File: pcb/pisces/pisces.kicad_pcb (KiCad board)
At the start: 2 copper layers, 149.9 x 66 mm, 51 parts, among them SW1 SW_PUSH, SW10 SW_PUSH, SW11 SW_PUSH, SW12 SW_PUSH, SW13 SW_PUSH, SW14 SW_PUSH, SW15 SW_PUSH, SW16 SW_PUSH, SW17 SW_PUSH, SW18 SW_PUSH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

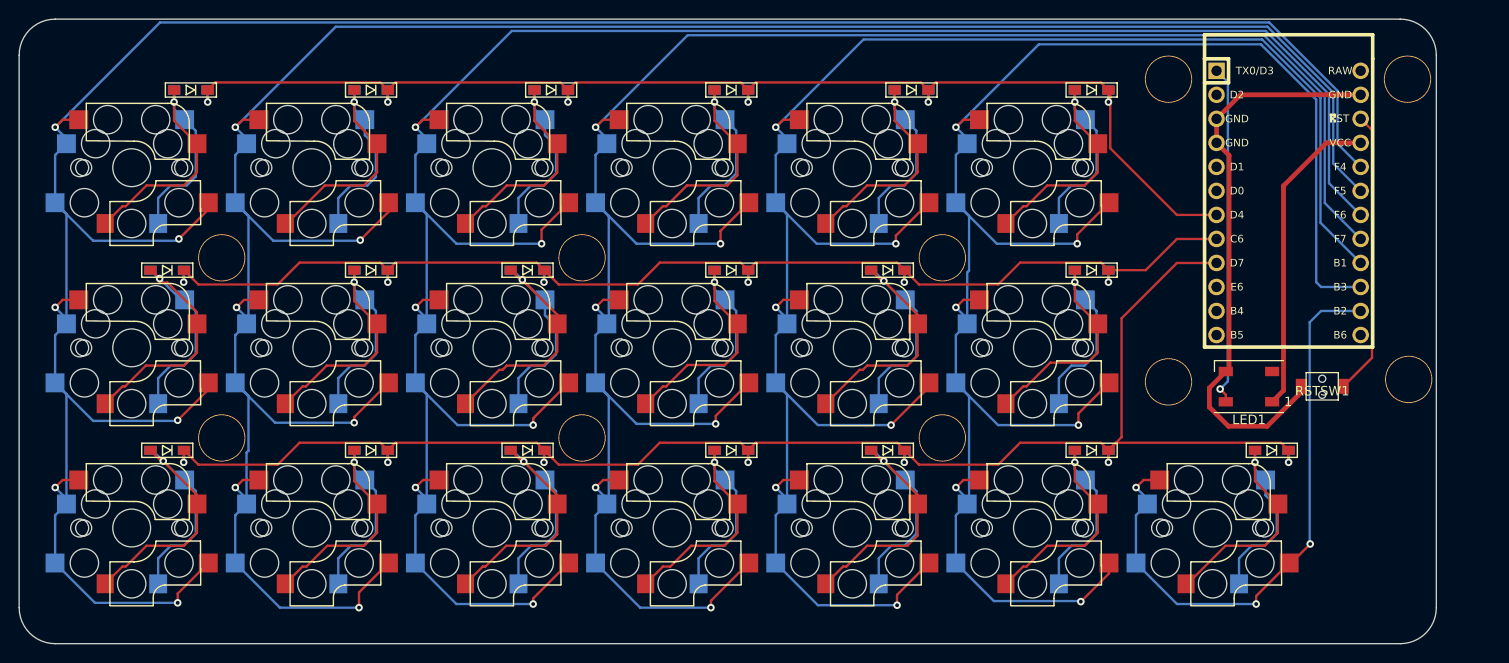
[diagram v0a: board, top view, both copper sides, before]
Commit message: Added a audio jack and connected tracks
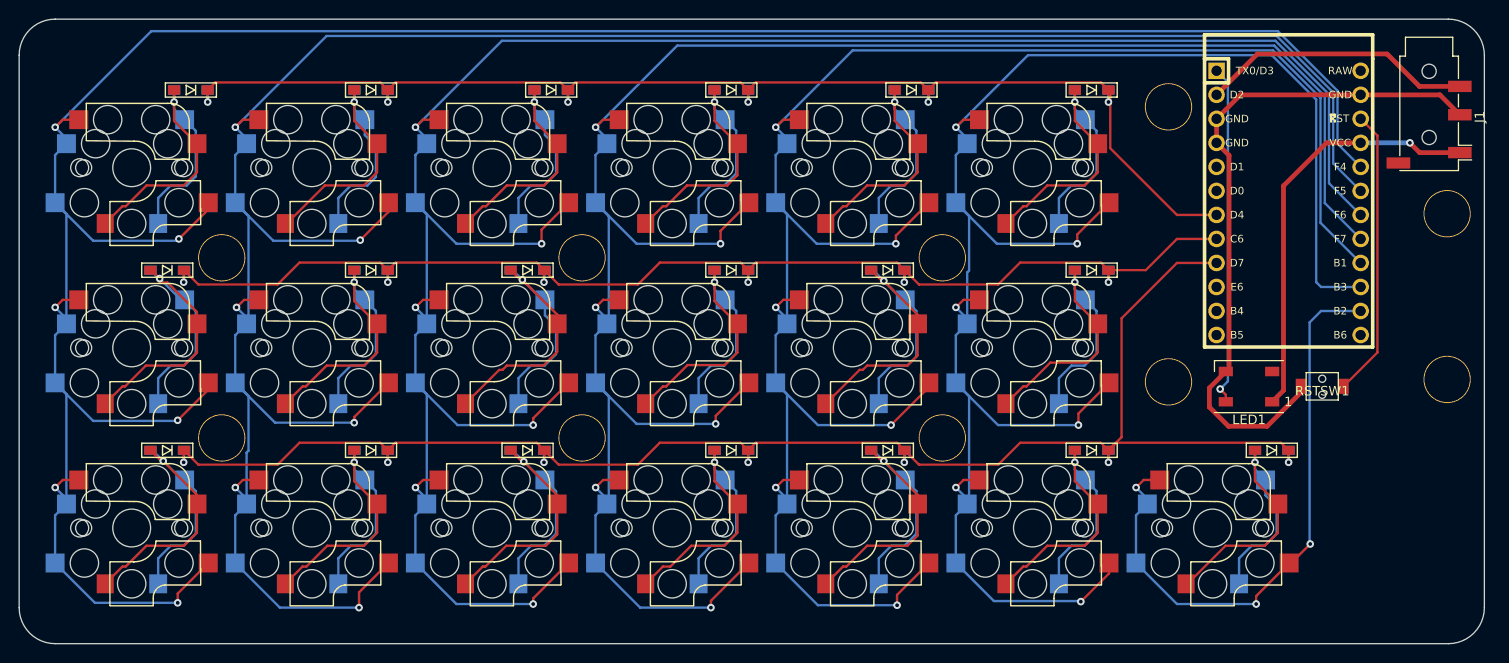
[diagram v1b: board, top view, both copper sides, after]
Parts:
- added J1: AudioJack4, Connector_Audio:Jack_3.5mm_PJ320D_Horizontal, F.Cu at (187.2, 44.6)
- moved Ref** 14.8 mm to (189.1, 54.9)
- moved Ref** 4.06 mm to (189.1, 72.4)
- moved Ref** 2.92 mm to (159.6, 43.6)
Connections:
- U1 pad 2: Net-(U1-Pad2) -> data
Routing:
- net data: track 0.00 -> 28.9 mm
- net GND: track 60.8 -> 72.2 mm
- net VCC: track 33.4 -> 44.3 mm, vias 0 -> 1
- net col4: track 206.2 -> 205.3 mm
- net col5: track 191.9 -> 191.0 mm
- net col3: track 224.2 -> 223.3 mm
- net col2: track 240.8 -> 240.0 mm
- net col1: track 258.3 -> 257.5 mm
- net col0: track 274.4 -> 273.6 mm
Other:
- board size 149.9 x 66 mm -> 154.9 x 66 mm

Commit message: Filled GND area
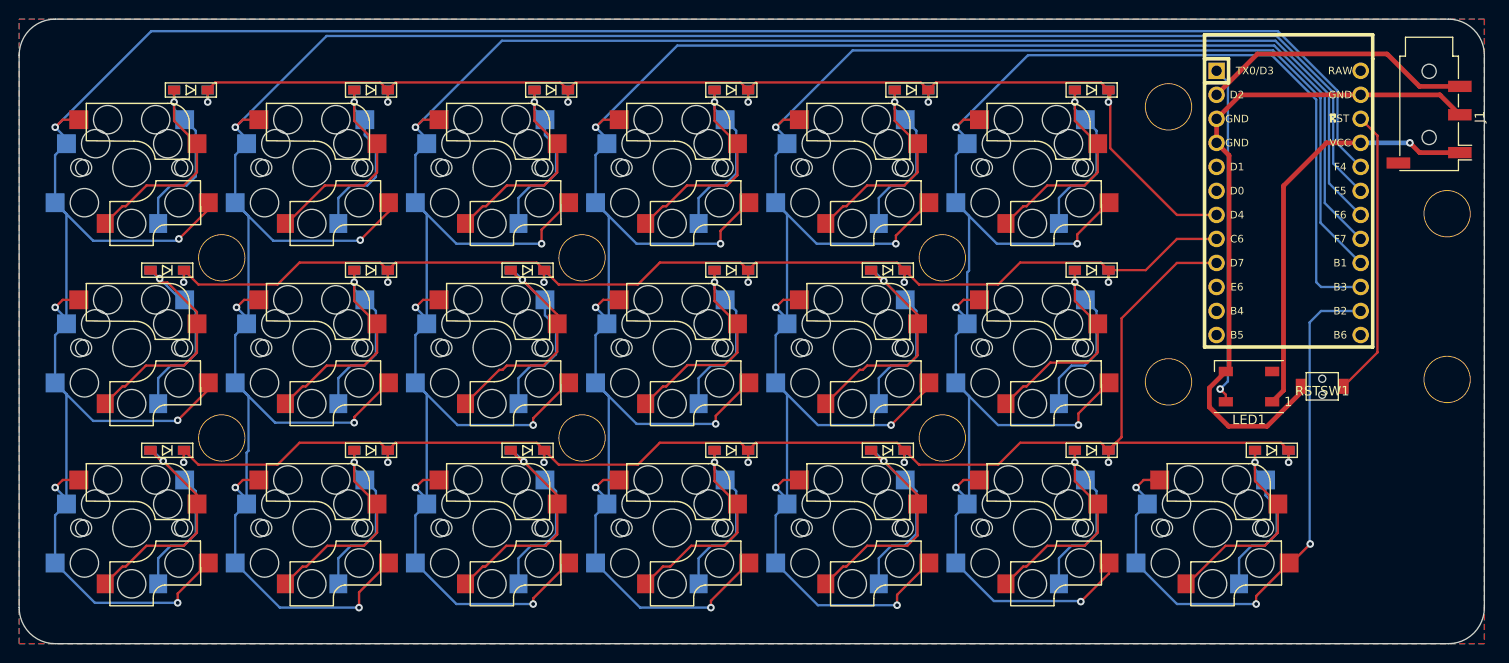
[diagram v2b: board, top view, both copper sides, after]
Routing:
- added copper zone on B.Cu, net GND
- added copper zone on F.Cu, net GND
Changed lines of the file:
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@@
   (segment (start 169.037 37.973) (end 182.753 37.973) (width 0.5) (layer F.Cu) (net 43))
   (segment (start 164.719 42.291) (end 169.037 37.973) (width 0.5) (layer F.Cu) (net 43))
+  (zone (net 23) (net_name GND) (layer F.Cu) (hatch edge 0.508)
+    (connect_pads (clearance 0.508))
+    (min_thickness 0.254)
+    (fill yes (arc_segments 32) (thermal_gap 0.508) (thermal_bridge_width 0.508))
+    (polygon
+      (pts
+        (xy 193.04 100.33) (xy 38.1 100.33) (xy 38.1 34.29) (xy 193.04 34.29)
+      )
+    )
+  )
+  (zone (net 23) (net_name GND) (layer B.Cu) (hatch edge 0.508)
+    (connect_pads (clearance 0.508))
+    (min_thickness 0.254)
+    (fill yes (arc_segments 32) (thermal_gap 0.508) (thermal_bridge_width 0.508))
+    (polygon
+      (pts
+        (xy 193.04 100.33) (xy 38.1 100.33) (xy 38.1 34.29) (xy 193.04 34.29)
+      )
+    )
+  )
 )

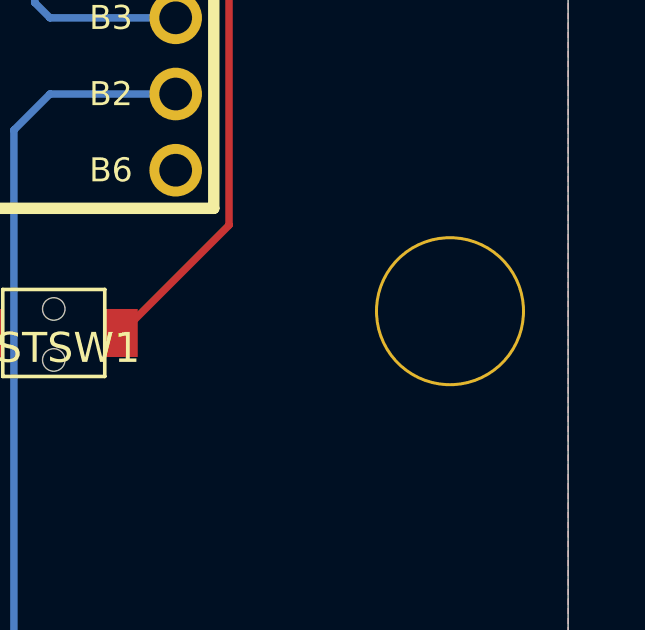
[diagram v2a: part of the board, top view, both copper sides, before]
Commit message: Aligned mounting holes
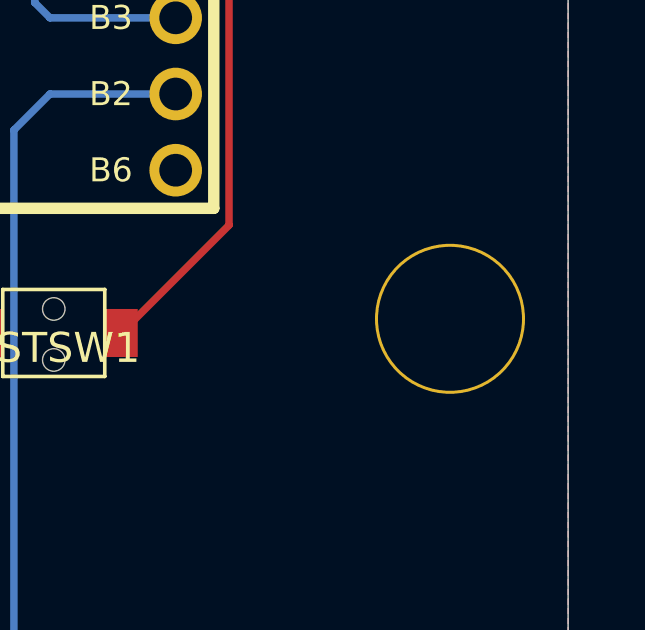
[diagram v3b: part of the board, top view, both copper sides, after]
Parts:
- moved Ref** 0.25 mm to (189.1, 72.6)
